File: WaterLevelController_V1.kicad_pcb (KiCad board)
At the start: 2 copper layers, 97.5 x 48 mm, 39 parts, among them J1 Screw_Terminal_01x02, J2 Screw_Terminal_01x02, J3 Screw_Terminal_01x02, J4 Screw_Terminal_01x02, K1 FINDER-40.52.9.012, K2 FINDER-40.52.9.012, Q1 BC547, Q2 BC557, SW1 SW_Push

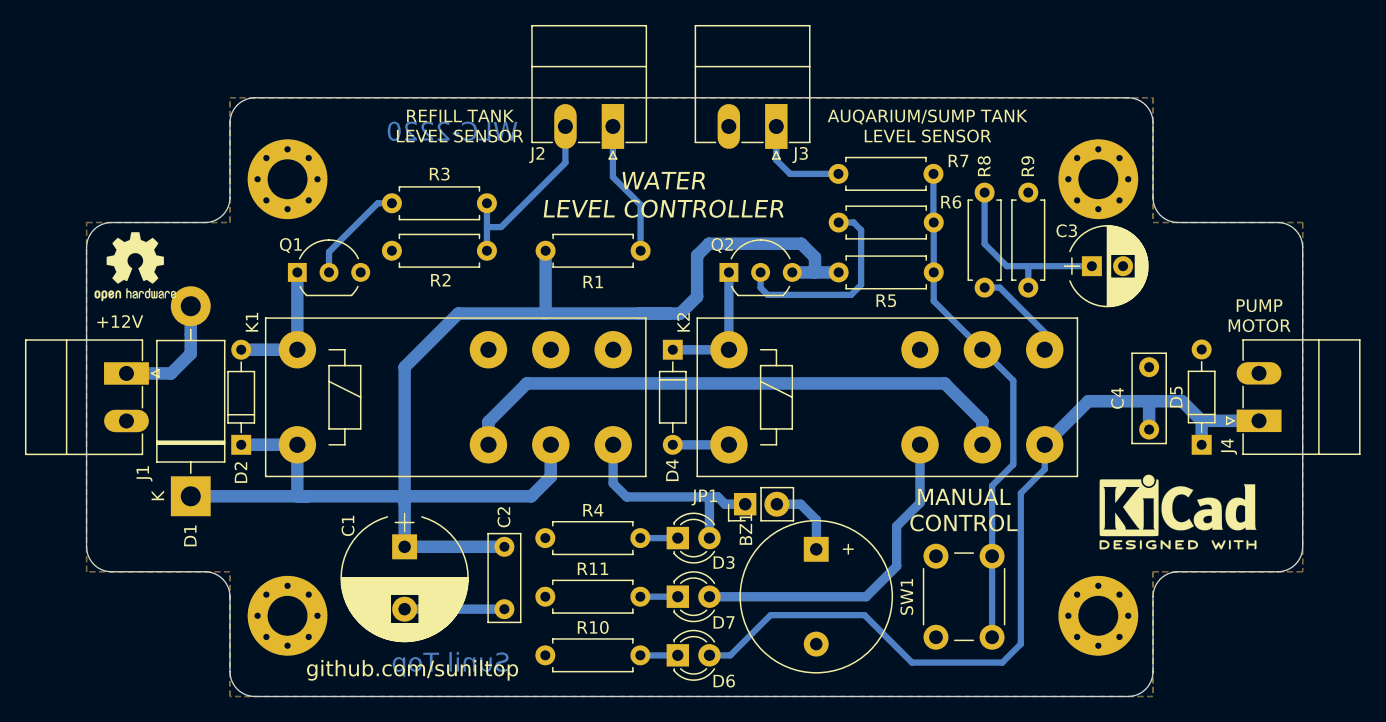
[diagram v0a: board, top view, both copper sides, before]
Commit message: Add files via upload
Added PTC type Resettable Fuse to voltage input
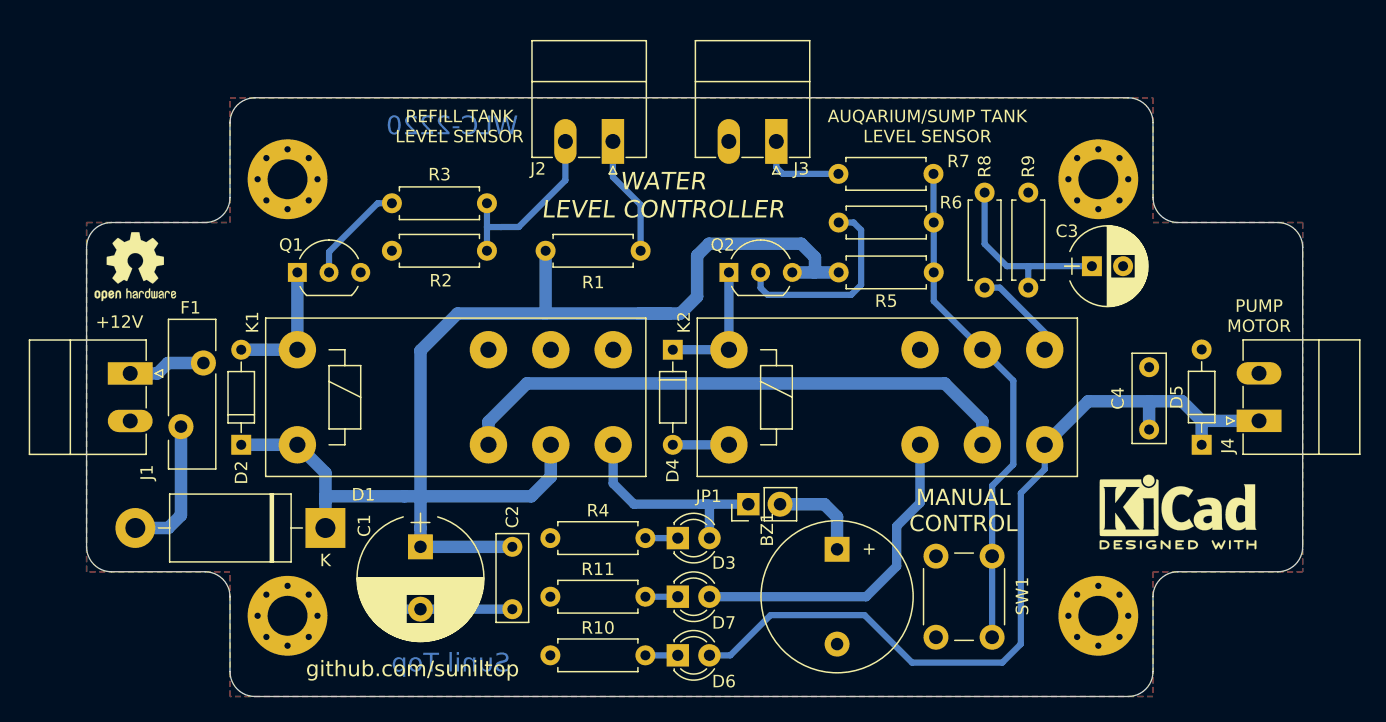
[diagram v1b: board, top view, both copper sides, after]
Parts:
- added F1: MF-R250, Fuse:Fuse_Bourns_MF-R250, F.Cu at (109.1, 102.4)
- moved D1 11.1 mm to (120.7, 110.5), turned to 180 degrees
- moved BZ1 1.67 mm to (161.7, 112.2)
- moved C1 1.27 mm to (128.3, 112.0)
- moved J2 1.20 mm to (143.7, 79.5)
- moved J3 1.20 mm to (156.8, 79.5)
- moved C2 0.64 mm to (135.6, 112.0)
- moved R10 0.40 mm to (146.3, 120.7)
- moved R11 0.40 mm to (146.3, 116.0)
- moved R4 0.40 mm to (138.7, 111.3)
- moved J1 0.30 mm to (105.0, 98.1)
- moved JP1 0.25 mm to (154.6, 108.6)
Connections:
- J1 pad 1: Net-(D1-Pad2) -> Net-(F1-Pad2)
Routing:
- net +12V: track 116.2 -> 106.4 mm
- net Net-(F1-Pad2): track 0.00 -> 6.29 mm
- net Net-(D1-Pad2): track 9.62 -> 11.2 mm
- net Net-(BZ1-Pad1): track 6.05 -> 7.59 mm
- net Net-(J2-Pad1): track 10.9 -> 9.69 mm
- net Net-(J3-Pad1): track 8.14 -> 7.28 mm
